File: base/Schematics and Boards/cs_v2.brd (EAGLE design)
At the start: 25.4 x 25.4 mm, 81 parts, among them J101 J-JTAG-CORTEX-NEEDLE6, J301 HIROSE-DF40_44-PIN_CONNECTORS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, J302 HIROSE-DF40_30-PIN_CONNECTORS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, Q201 FK3303010L, Q202 FK3303010L, Q203 FK3303010L, Q204 DMG3415UFY4Q-7, U1 AT25SF641-MHB-T, U101 ATSAMD51, U201 COULOMB-MAX17262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

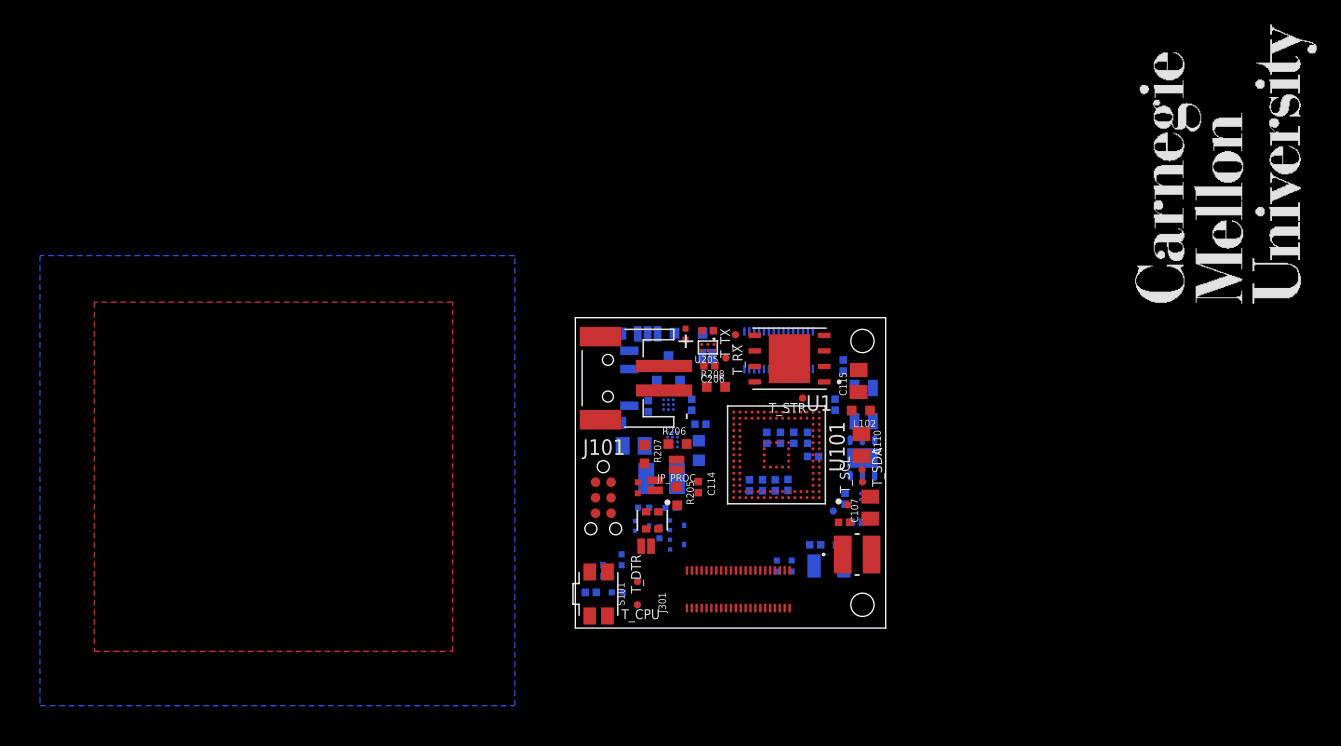
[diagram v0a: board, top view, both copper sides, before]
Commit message: Re-place a few components and prep for routing
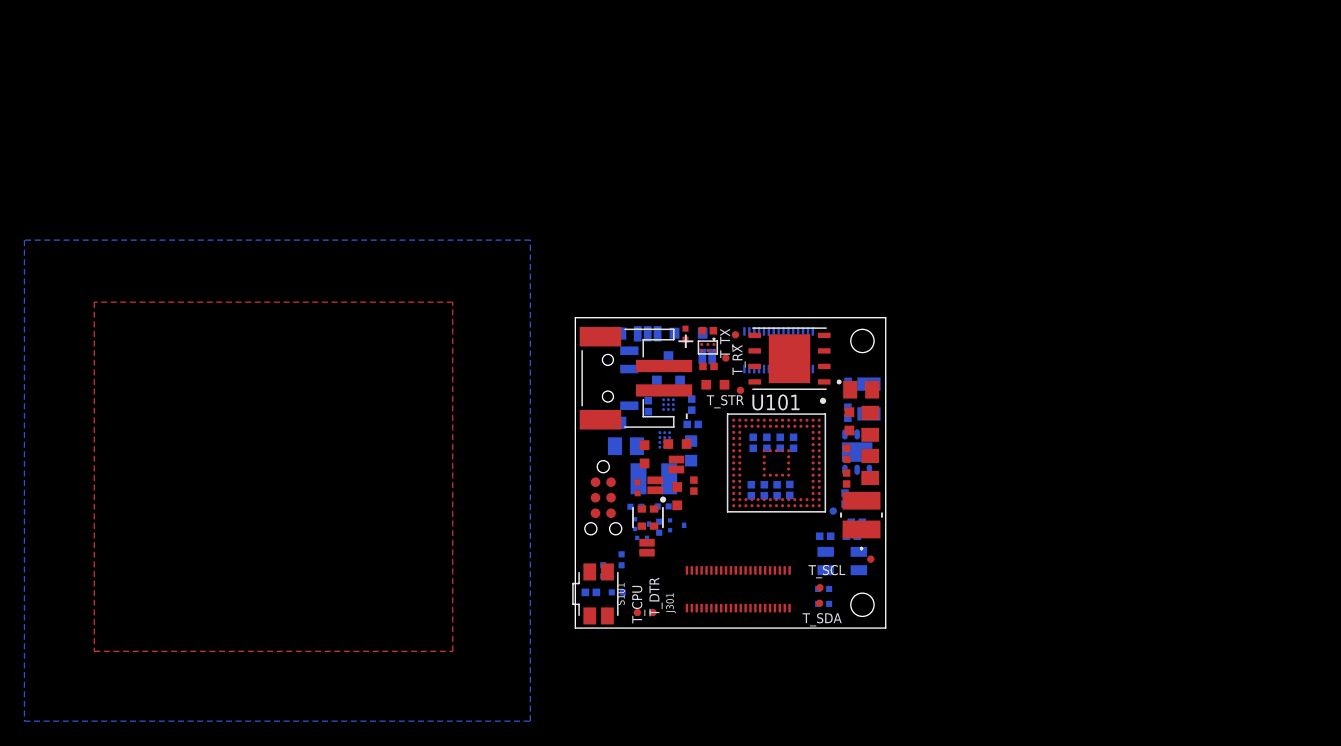
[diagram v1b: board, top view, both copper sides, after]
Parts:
- removed U$1: (no value), Graphics:CMU_LOGO
- moved Y102 14.1 mm to (24.0, 18.7), turned to 90 degrees
- moved C116 14.0 mm to (20.4, 7.52), turned to 180 degrees
- moved C119 13.2 mm to (22.3, 19.7), turned to 90 degrees
- moved Y101 12.9 mm to (21.8, 5.49), turned to 180 degrees
- moved T_SDA 11.5 mm to (20.0, 2.03), turned to 0 degrees
- moved C117 10.9 mm to (22.6, 7.52), turned to 180 degrees
- moved C118 10.8 mm to (22.3, 17.6), turned to 270 degrees
- moved T_SCL 9.33 mm to (20.0, 3.30), turned to 0 degrees
- moved T_STR 5.12 mm to (13.5, 19.5)
- moved T_COR 4.84 mm to (24.2, 5.64)
- moved R104 4.27 mm to (20.3, 3.20), turned to 180 degrees
- moved R103 4.06 mm to (20.3, 1.98), turned to 180 degrees
- moved C103 3.59 mm to (22.2, 12.2), turned to 270 degrees
- moved C108 3.48 mm to (22.2, 14.3), flipped to the top, turned to 270 degrees
- moved C107 3.33 mm to (24.1, 13.2), turned to 270 degrees
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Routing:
- added copper zone on layer 13, net +3V3_PROC
- added copper zone on layer 15, net GND
- removed copper zone on layer 15, net +3V3_PROC

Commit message: Manual route power traces, lock traces/vias before autoroute
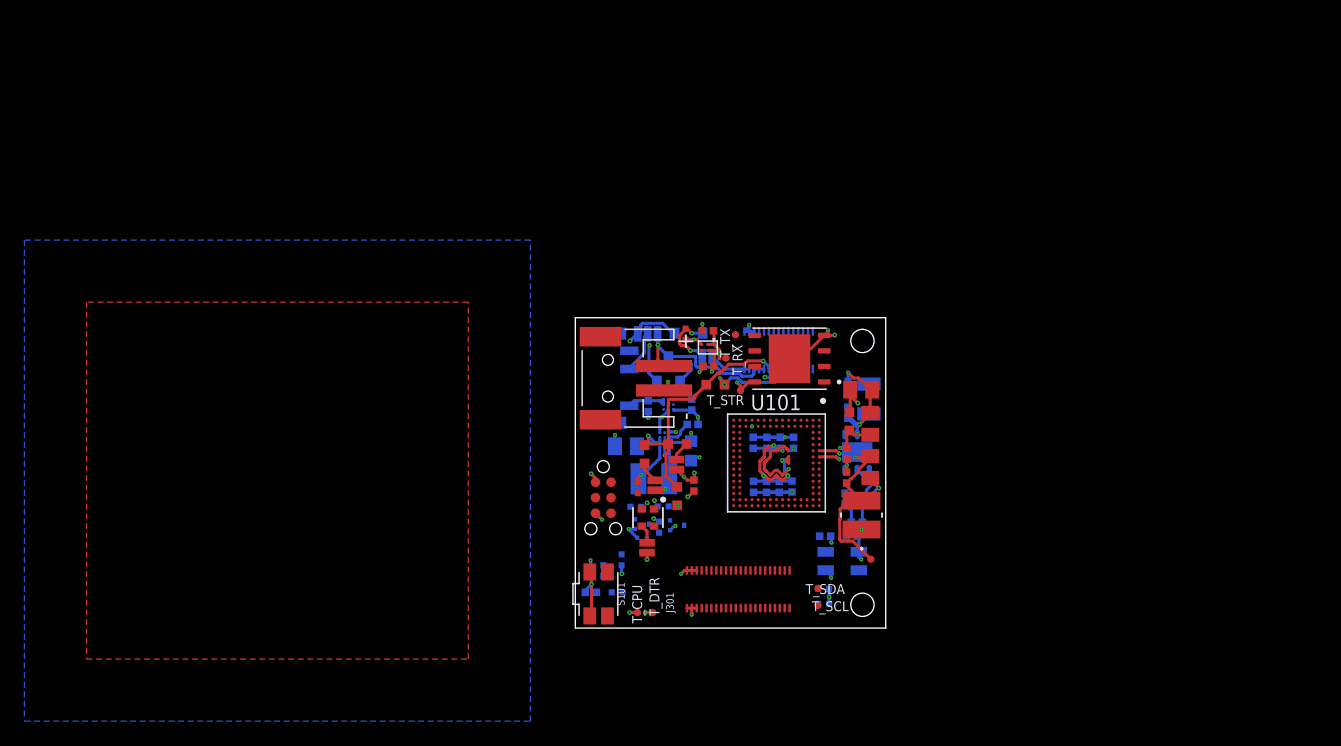
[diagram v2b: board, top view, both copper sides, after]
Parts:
- moved T_TMP 4.10 mm to (24.5, 11.9)
- moved T_SCL 1.46 mm to (19.9, 1.85), turned to 180 degrees
- moved T_SDA 1.23 mm to (19.9, 3.25)
- moved C112 0.33 mm to (14.6, 11.6)
- moved C113 0.33 mm to (15.6, 11.6)
- moved C111 0.33 mm to (16.7, 11.6)
- moved C109 0.33 mm to (17.7, 11.6)
- moved C103 0.08 mm to (22.2, 12.3), turned to 90 degrees
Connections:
- net DTR_DETECT: now also U101.PA21; no longer U101.PC31
- net EN_TEMP: now also U101.PB25; no longer U101.PC07
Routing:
- net GND: track 0.00 -> 130.1 mm, vias 0 -> 35
- net +3V3_PROC: track 0.00 -> 74.2 mm, vias 0 -> 16
- net +3V3_TEMP_SENSE: track 0.00 -> 52.8 mm, vias 0 -> 7
- net +3V3_DTR: track 0.00 -> 46.7 mm, vias 0 -> 7
- net +3V3: track 0.00 -> 23.6 mm, vias 0 -> 2
- net VDDCORE: track 0.00 -> 17.1 mm, vias 0 -> 4
- net VDDANA: track 0.00 -> 14.2 mm, vias 0 -> 7
- net +3V7_BATT: track 0.00 -> 13.6 mm, vias 0 -> 1
- net VSW: track 0.00 -> 13.4 mm, vias 0 -> 4
- net VDD_SW: track 0.00 -> 10.0 mm, vias 0 -> 3
- net +3V3_STOR_SENSE: track 0.00 -> 9.77 mm, vias 0 -> 5
- net +3V3_STOR: track 0.00 -> 8.44 mm, vias 0 -> 4
- net VDD_DBG_JMP: track 0.00 -> 8.26 mm, vias 0 -> 4
- net VREG_IN: track 0.00 -> 7.59 mm, vias 0 -> 4
- net CC_IN: track 0.00 -> 3.83 mm
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
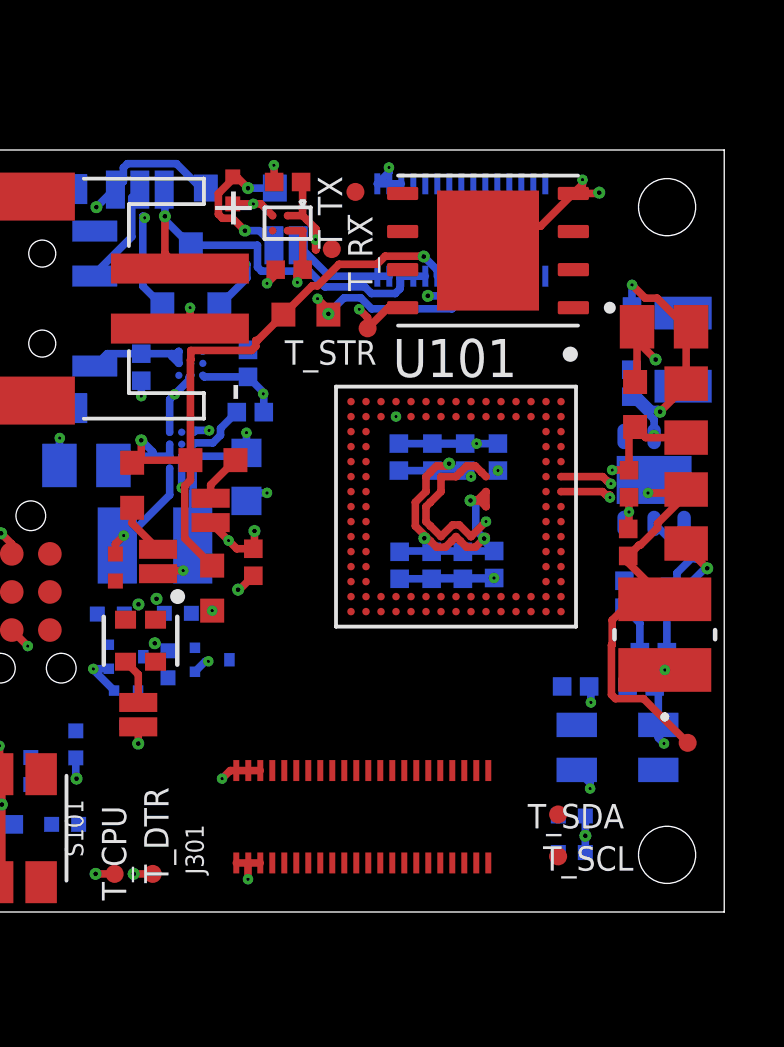
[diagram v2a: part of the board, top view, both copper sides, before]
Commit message: Escape for BGA signals with microvia in pad
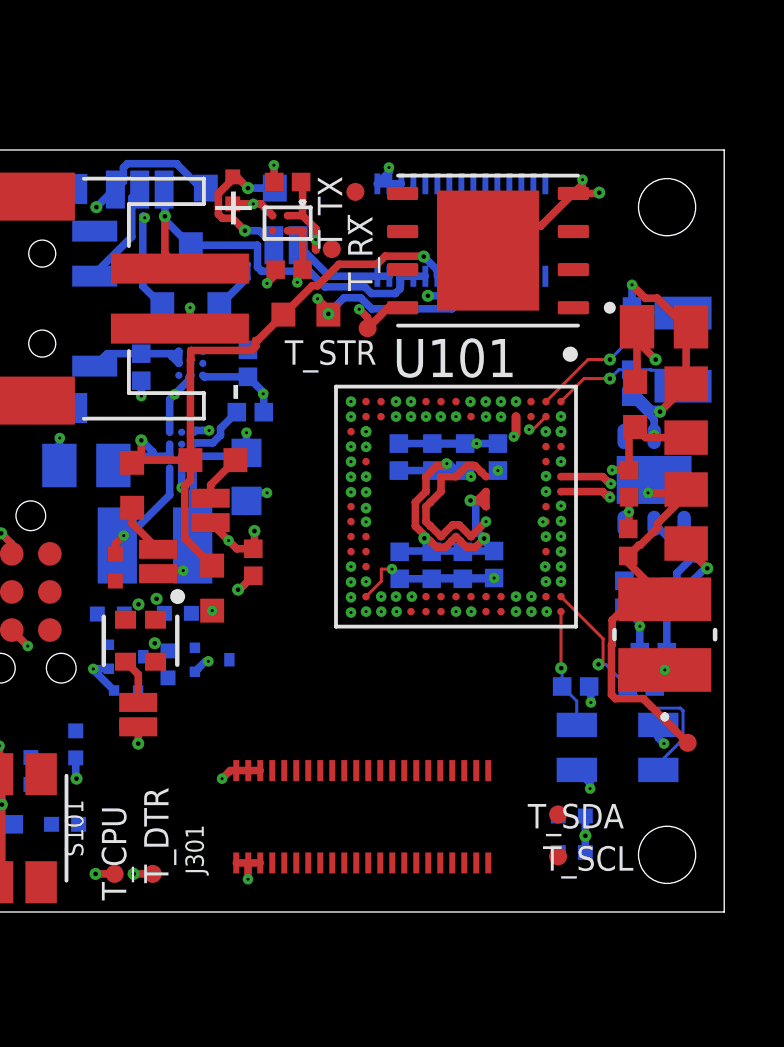
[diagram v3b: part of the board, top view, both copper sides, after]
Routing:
- net XOUT: track 0.00 -> 8.83 mm, vias 0 -> 1
- net XOUT32: track 0.00 -> 5.87 mm, vias 0 -> 1
- net GND: track 130.1 -> 134.9 mm, vias 35 -> 38
- net XIN32: track 0.00 -> 4.74 mm, vias 0 -> 1
- net XIN: track 0.00 -> 4.02 mm, vias 0 -> 1
- net DTR_BUS1_SERCOM1_P1: track 0.00 -> 1.48 mm, vias 0 -> 2
- net STOR_SPI5_MISO: track 0.00 -> 0.79 mm, vias 0 -> 2
- net DTR_BUS3_GPIO0: track 0.00 -> 0.59 mm, vias 0 -> 2
- net DBG_GPIO3: track 0.00 -> 0.59 mm, vias 0 -> 2
- net DBG_SWDIO: track 0.00 -> 0.53 mm, vias 0 -> 2
- net DTR_BUS3_SERCOM7_P1: track 0.00 -> 0.51 mm, vias 0 -> 2
- net DTR_BUS2_SERCOM2_P1: track 0.00 -> 0.48 mm, vias 0 -> 2
- net DBG_SERIAL_TX: track 0.00 -> 0.47 mm, vias 0 -> 2
- net DBG_TRACE_SWO: track 0.00 -> 0.45 mm, vias 0 -> 2
- net DTR_BUS0_SERCOM0_P0: track 0.00 -> 0.41 mm, vias 0 -> 2
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
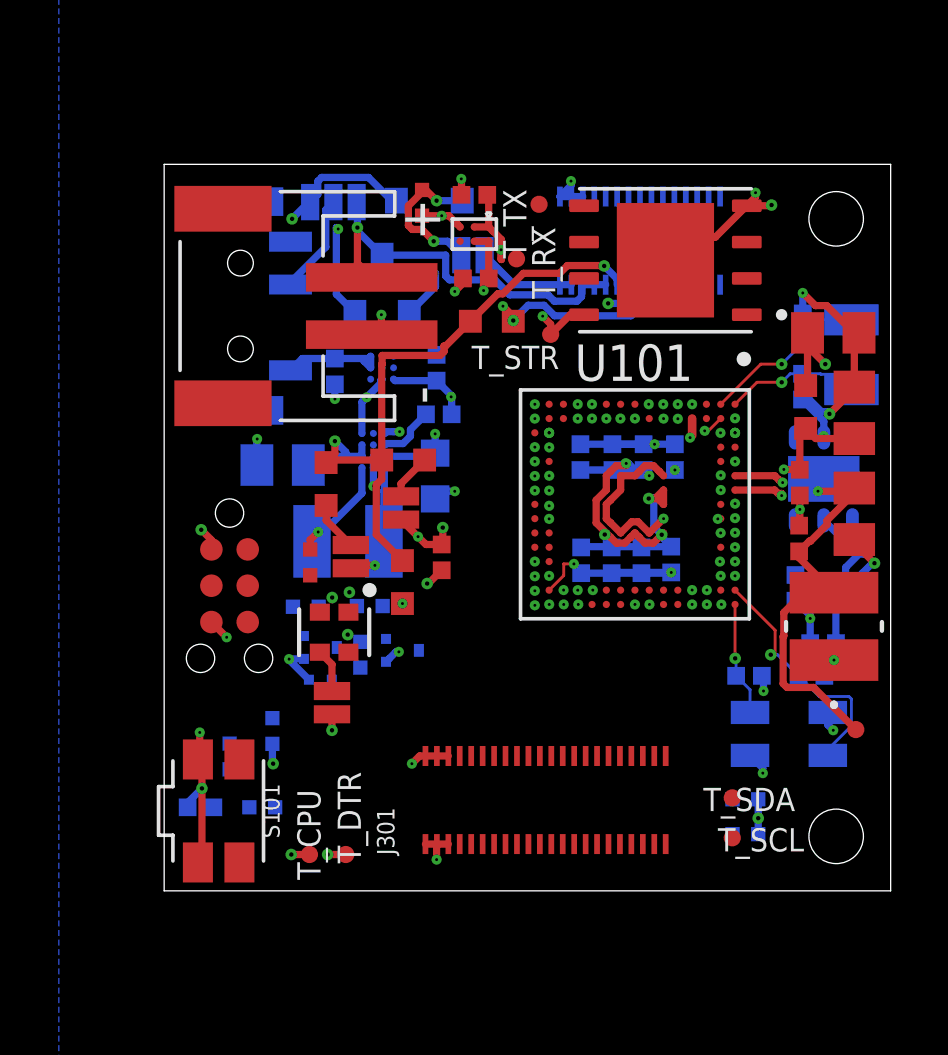
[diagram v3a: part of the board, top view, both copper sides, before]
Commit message: Autorouted board 100%. No DRC check
Considering a full manual route to decrease some trace lengths and reduce via count (>400)
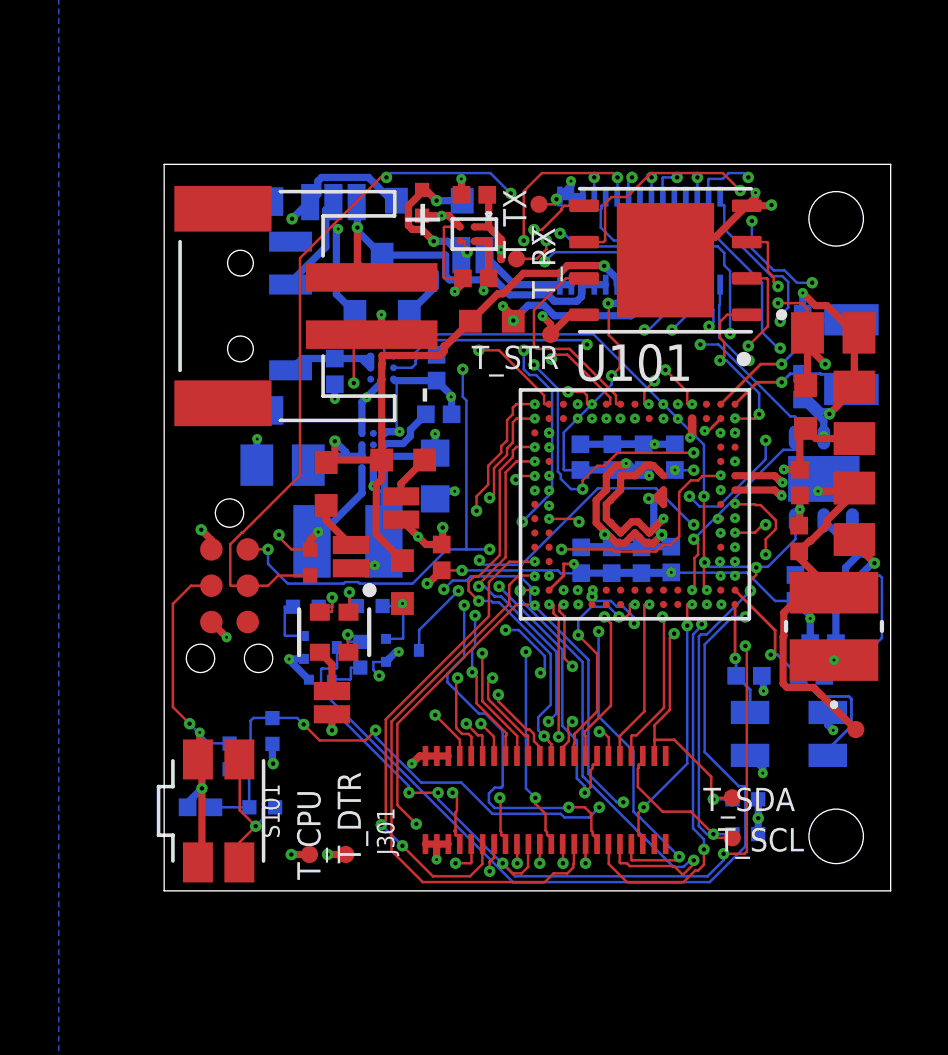
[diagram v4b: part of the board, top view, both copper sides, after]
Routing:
- net DBG_SWCLK: track 0.03 -> 46.3 mm, vias 2 -> 8
- net NRESET: track 0.03 -> 42.2 mm, vias 2 -> 8
- net DTR_MASTER_I2C_SCL: track 0.02 -> 39.5 mm, vias 2 -> 7
- net DBG_SWDIO: track 0.53 -> 38.3 mm, vias 2 -> 9
- net DTR_MASTER_I2C_SDA: track 0.01 -> 34.5 mm, vias 2 -> 7
- net DBG_USB_D+: track 0.03 -> 33.5 mm, vias 2 -> 4
- net LED_B: track 0.02 -> 32.0 mm, vias 2 -> 3
- net DBG_GPIO0: track 0.02 -> 30.8 mm, vias 2 -> 8
- net DTR_BUS2_AIN0: track 0.02 -> 29.6 mm, vias 2 -> 6
- net DBG_GPIO1: track 0.04 -> 29.2 mm, vias 2 -> 8
- net LED_R: track 0.02 -> 27.9 mm, vias 2 -> 6
- net DTR_BUS3_AIN0: track 0.01 -> 27.8 mm, vias 2 -> 4
- net DTR_BUS0_AIN0: track 0.00 -> 27.5 mm, vias 2 -> 5
- net GND: track 134.9 -> 160.0 mm, vias 38 -> 41
- net DTR_BUS2_AIN1: track 0.33 -> 25.2 mm, vias 2 -> 4
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
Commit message: Attempt to hand route signals; about 30% done w/ BGA
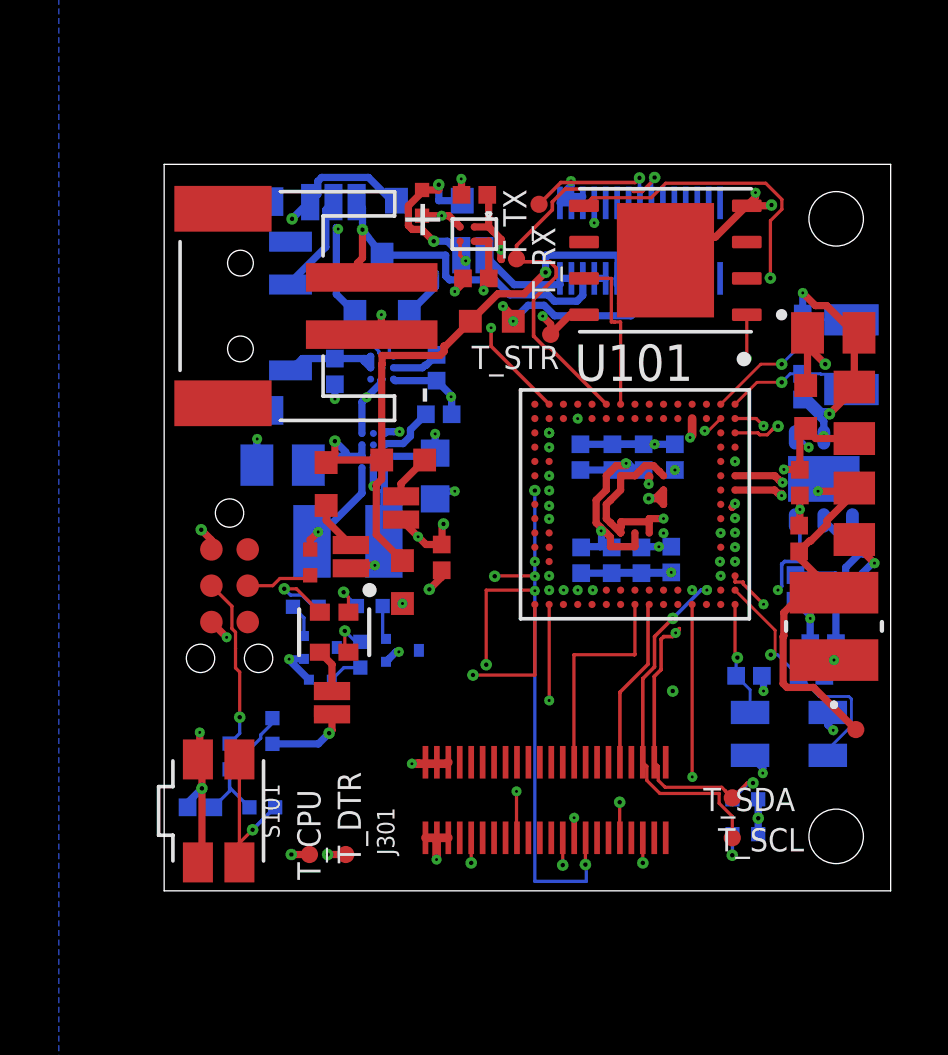
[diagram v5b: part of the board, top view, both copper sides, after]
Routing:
- net DBG_SWCLK: track 46.3 -> 2.33 mm, vias 8 -> 0
- net DBG_SWDIO: track 38.3 -> 0.00 mm, vias 9 -> 0
- net NRESET: track 42.2 -> 5.91 mm, vias 8 -> 2
- net DTR_MASTER_I2C_SDA: track 34.5 -> 68.5 mm, vias 7 -> 10
- net DBG_USB_D+: track 33.5 -> 0.01 mm, vias 4 -> 0
- net LED_B: track 32.0 -> 0.02 mm, vias 3 -> 2
- net DBG_GPIO0: track 30.8 -> 0.71 mm, vias 8 -> 2
- net DTR_BUS2_AIN0: track 29.6 -> 0.00 mm, vias 6 -> 0
- net DBG_GPIO1: track 29.2 -> 0.04 mm, vias 8 -> 2
- net DTR_BUS3_AIN0: track 27.8 -> 0.00 mm, vias 4 -> 0
- net DTR_BUS0_AIN0: track 27.5 -> 0.00 mm, vias 5 -> 0
- net DTR_BUS2_AIN1: track 25.2 -> 0.00 mm, vias 4 -> 0
- net DTR_BUS3_AIN1: track 24.5 -> 0.00 mm, vias 5 -> 0
- net DTR_BUS0_SERCOM0_P3: track 24.4 -> 0.00 mm, vias 4 -> 1
- net DTR_BUS0_SERCOM0_P0: track 21.9 -> 0.00 mm, vias 5 -> 0
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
